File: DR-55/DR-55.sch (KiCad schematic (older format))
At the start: 0 parts

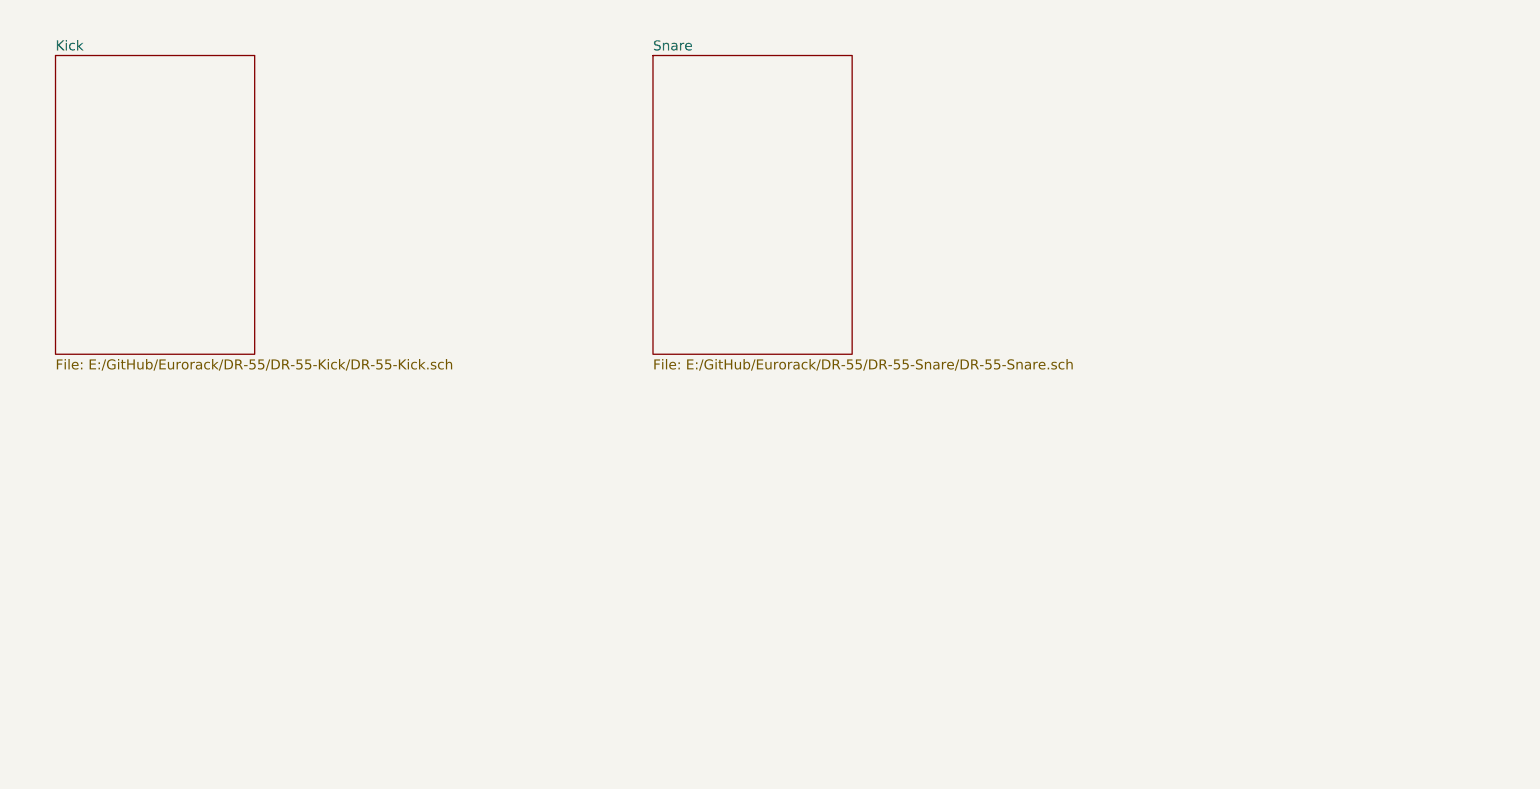
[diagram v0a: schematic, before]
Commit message: Added drums
Added all drum schematics.
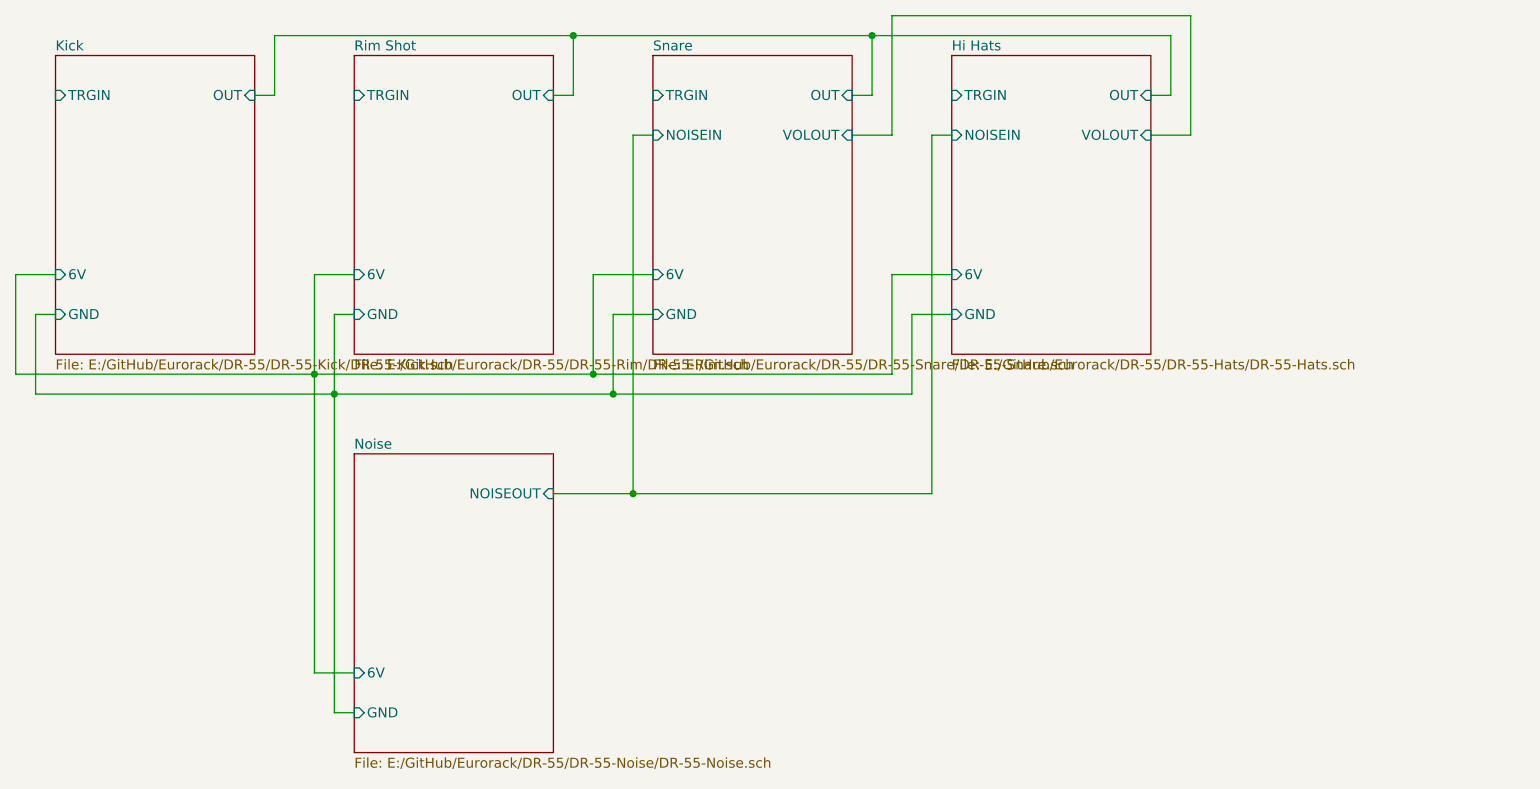
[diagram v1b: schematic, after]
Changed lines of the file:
@@
 $Descr A4 11693 8268
 encoding utf-8
-Sheet 1 3
+Sheet 1 6
 Title ""
 Date ""
@@
 F0 "Kick" 50
 F1 "E:/GitHub/Eurorack/DR-55/DR-55-Kick/DR-55-Kick.sch" 50
+F2 "OUT" I R 2500 1700 50
+F3 "TRGIN" I L 1500 1700 50
+F4 "6V" I L 1500 2600 50
+F5 "GND" I L 1500 2800 50
 $EndSheet
 $Sheet
@@
 F0 "Snare" 50
 F1 "E:/GitHub/Eurorack/DR-55/DR-55-Snare/DR-55-Snare.sch" 50
+F2 "TRGIN" I L 4500 1700 50
+F3 "GND" I L 4500 2800 50
+F4 "OUT" I R 5500 1700 50
+F5 "6V" I L 4500 2600 50
+F6 "VOLOUT" I R 5500 1900 50
+F7 "NOISEIN" I L 4500 1900 50
 $EndSheet
+$Sheet
+S 6000 1500 1000 1500
+U 627D8A3A
+F0 "Hi Hats" 50
+F1 "E:/GitHub/Eurorack/DR-55/DR-55-Hats/DR-55-Hats.sch" 50
+F2 "TRGIN" I L 6000 1700 50
+F3 "GND" I L 6000 2800 50
+F4 "NOISEIN" I L 6000 1900 50
+F5 "OUT" I R 7000 1700 50
+F6 "VOLOUT" I R 7000 1900 50
+F7 "6V" I L 6000 2600 50
+$EndSheet
+$Sheet
+S 3000 3500 1000 1500
+U 62804B1F
+F0 "Noise" 50
+F1 "E:/GitHub/Eurorack/DR-55/DR-55-Noise/DR-55-Noise.sch" 50
+F2 "GND" I L 3000 4800 50
+F3 "6V" I L 3000 4600 50
+F4 "NOISEOUT" I R 4000 3700 50
+$EndSheet
+Wire Wire Line
+	4400 3700 4000 3700
+Wire Wire Line
+	4400 3700 4400 1900
+Wire Wire Line
+	4400 1900 4500 1900
+Wire Wire Line
+	4400 3700 5900 3700
+Wire Wire Line
+	5900 3700 5900 1900
+Wire Wire Line
+	5900 1900 6000 1900
+Connection ~ 4400 3700
+Wire Wire Line
+	1500 2600 1300 2600
+Wire Wire Line
+	1300 2600 1300 3100
+Wire Wire Line
+	5700 3100 5700 2600
+Wire Wire Line
+	5700 2600 6000 2600
+Wire Wire Line
+	1300 3100 2800 3100
+Wire Wire Line
+	3000 2600 2800 2600
+Wire Wire Line
+	2800 2600 2800 3100
+Connection ~ 2800 3100
+Wire Wire Line
+	3000 2800 2900 2800
+Wire Wire Line
+	2900 2800 2900 3200
+Wire Wire Line
+	2900 3200 1400 3200
+Wire Wire Line
+	1400 3200 1400 2800
+Wire Wire Line
+	1400 2800 1500 2800
+$Sheet
+S 3000 1500 1000 1500
+U 62804339
+F0 "Rim Shot" 50
+F1 "E:/GitHub/Eurorack/DR-55/DR-55-Rim/DR-55-Rim.sch" 50
+F2 "TRGIN" I L 3000 1700 50
+F3 "GND" I L 3000 2800 50
+F4 "OUT" I R 4000 1700 50
+F5 "6V" I L 3000 2600 50
+$EndSheet
+Wire Wire Line
+	2800 3100 4200 3100
+Wire Wire Line
+	4500 2600 4200 2600
+Wire Wire Line
+	4200 2600 4200 3100
+Connection ~ 4200 3100
+Wire Wire Line
+	4200 3100 5700 3100
+Wire Wire Line
+	4500 2800 4300 2800
+Wire Wire Line
+	4300 2800 4300 3200
+Wire Wire Line
+	4300 3200 2900 3200
+Connection ~ 2900 3200
+Wire Wire Line
+	4300 3200 5800 3200
+Wire Wire Line
+	5800 3200 5800 2800
+Wire Wire Line
+	5800 2800 6000 2800
+Connection ~ 4300 3200
+Wire Wire Line
+	2500 1700 2600 1700
+Wire Wire Line
+	2600 1700 2600 1400
+Wire Wire Line
+	2600 1400 4100 1400
+Wire Wire Line
+	4100 1400 4100 1700
+Wire Wire Line
+	4100 1700 4000 1700
+Wire Wire Line
+	4100 1400 5600 1400
+Wire Wire Line
+	5600 1400 5600 1700
+Wire Wire Line
+	5600 1700 5500 1700
+Connection ~ 4100 1400
+Wire Wire Line
+	5600 1400 7100 1400
+Wire Wire Line
+	7100 1400 7100 1700
+Wire Wire Line
+	7100 1700 7000 1700
+Connection ~ 5600 1400
+Wire Wire Line
+	7000 1900 7200 1900
+Wire Wire Line
+	7200 1900 7200 1300
+Wire Wire Line
+	7200 1300 5700 1300
+Wire Wire Line
+	5700 1900 5700 1300
+Wire Wire Line
+	5500 1900 5700 1900
+Wire Wire Line
+	3000 4600 2800 4600
+Wire Wire Line
+	2800 4600 2800 3100
+Wire Wire Line
+	3000 4800 2900 4800
+Wire Wire Line
+	2900 4800 2900 3200
 $EndSCHEMATC

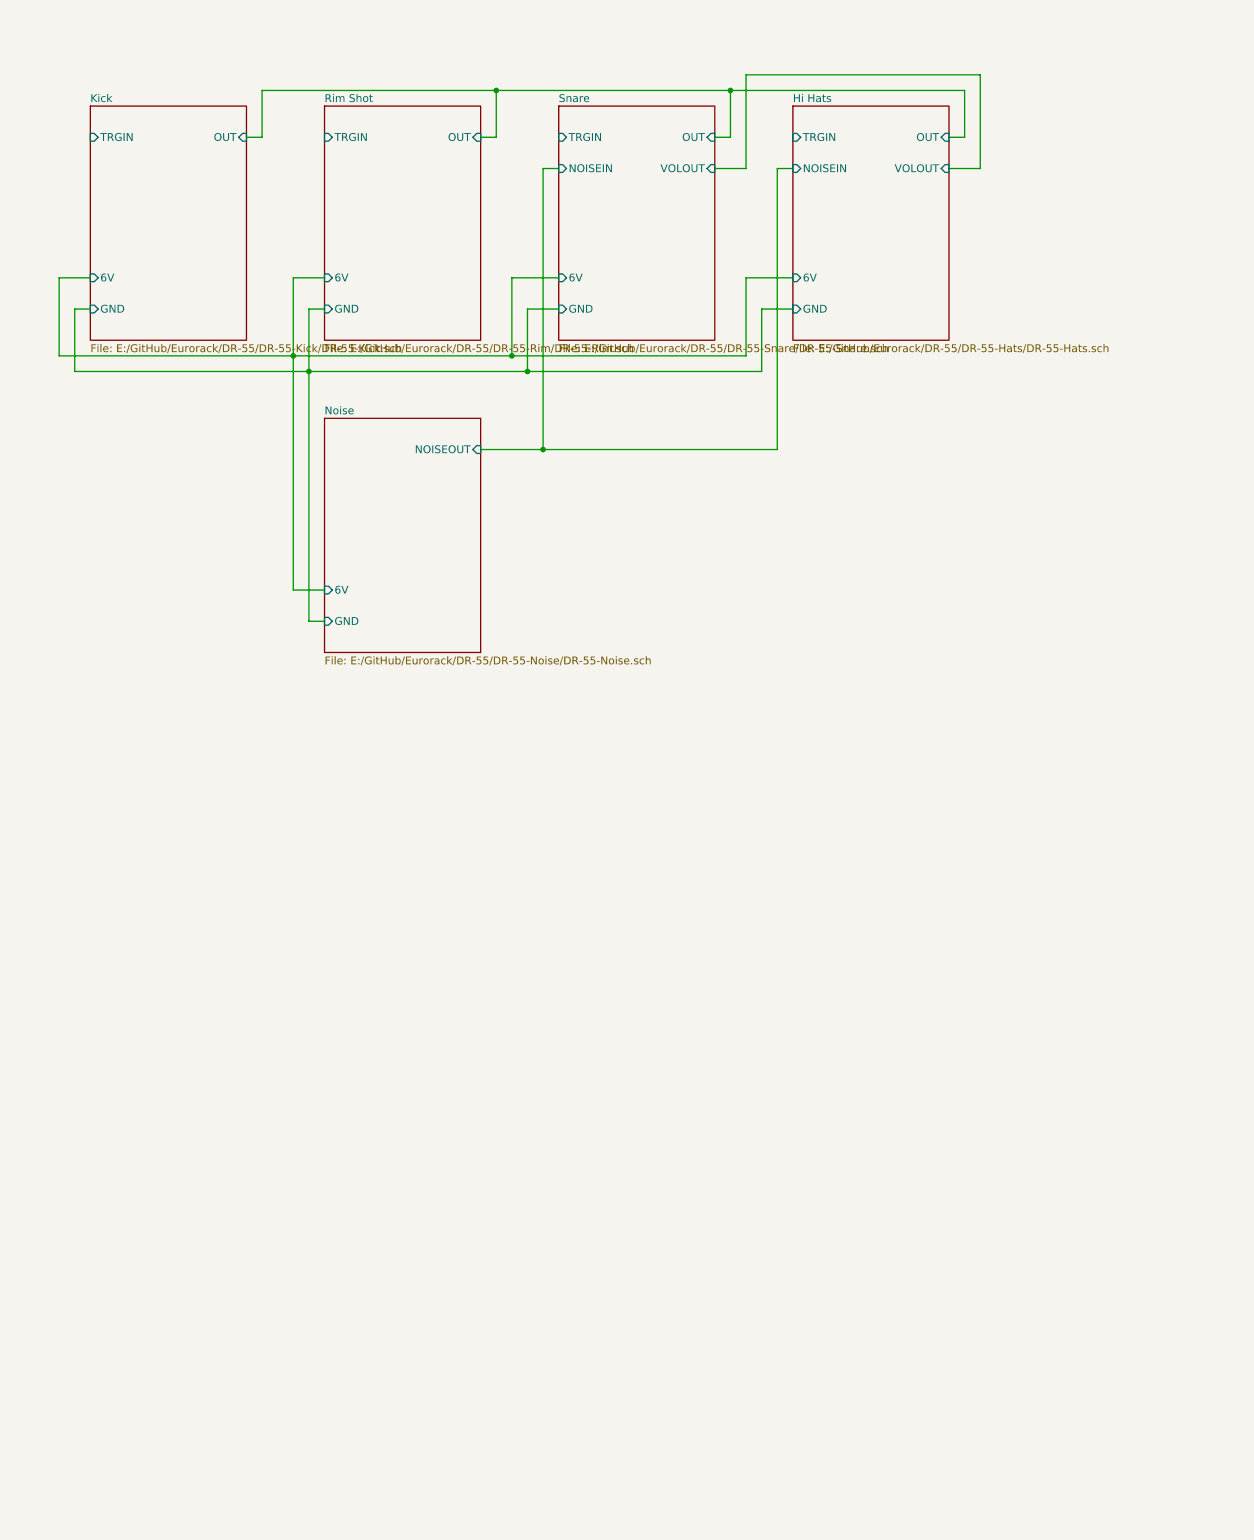
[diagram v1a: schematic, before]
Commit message: rearrange submodules
rearrange hirachial schematics in the main view.
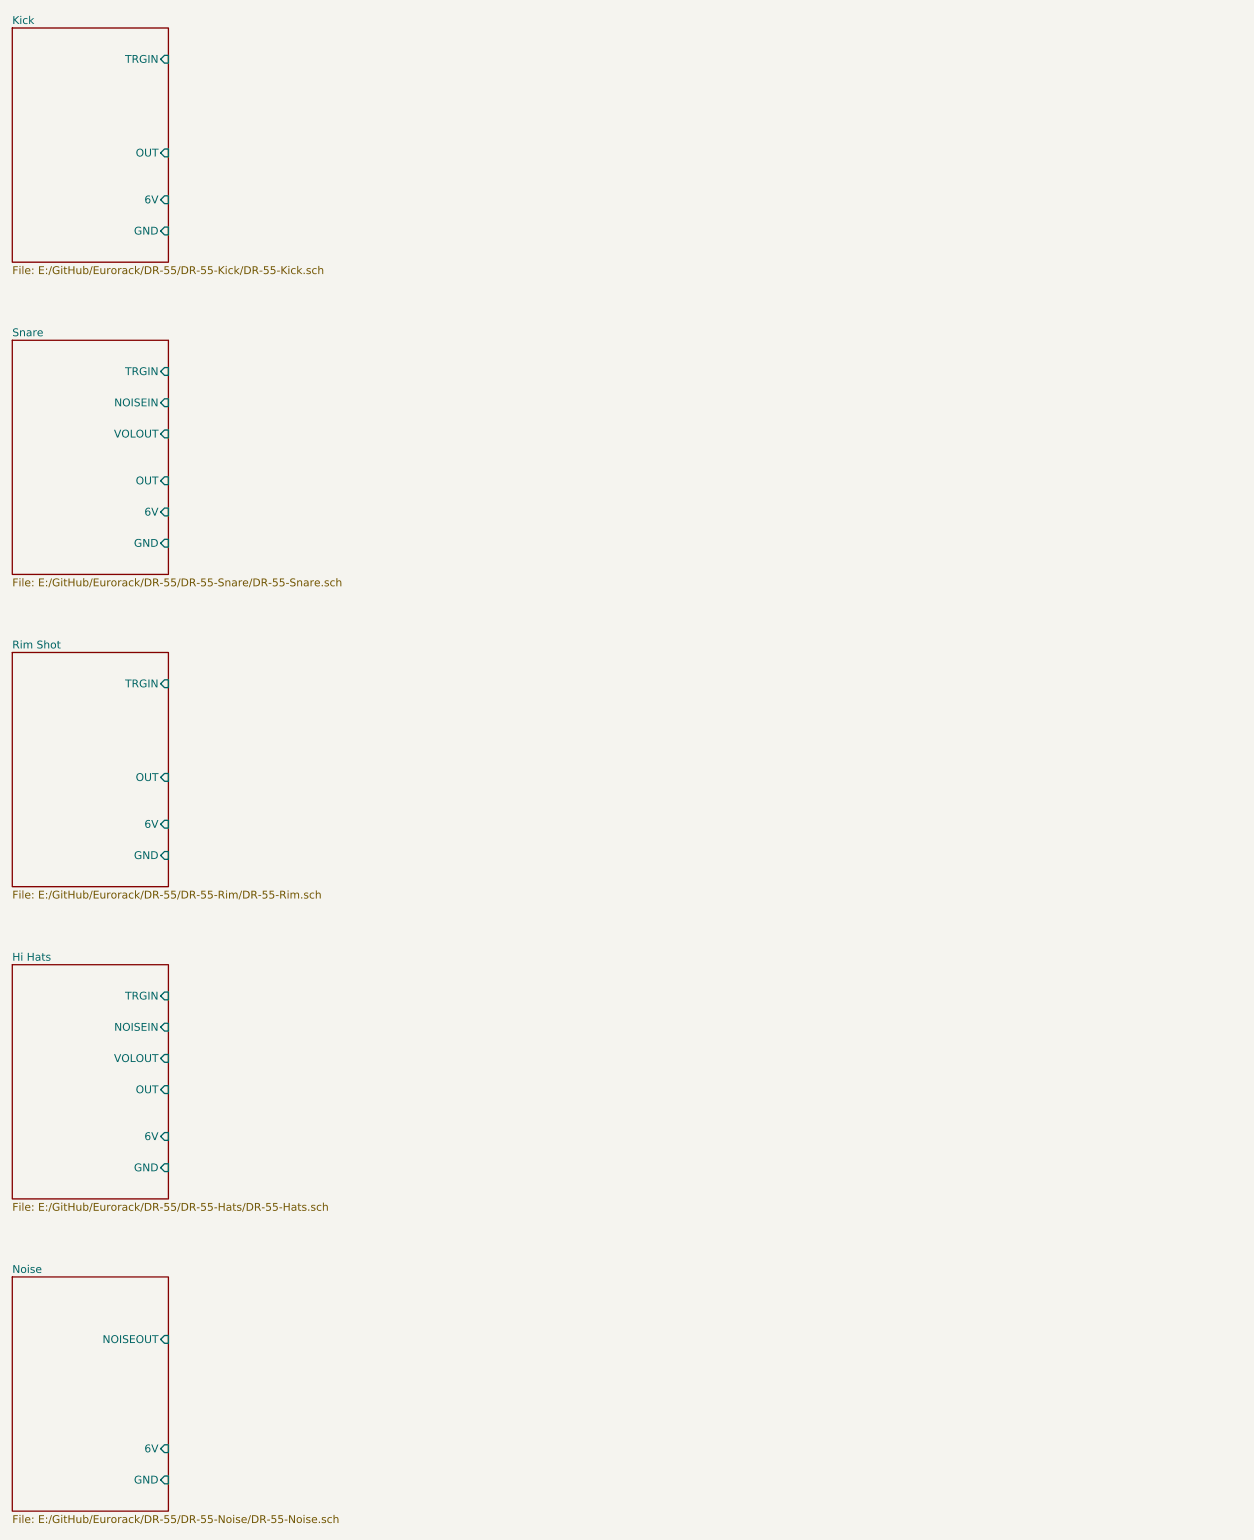
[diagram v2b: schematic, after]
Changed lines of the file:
@@
 EELAYER 30 0
 EELAYER END
-$Descr A4 11693 8268
+$Descr A3 16535 11693
 encoding utf-8
 Sheet 1 6
@@
 $EndDescr
 $Sheet
-S 1500 1500 1000 1500
+S 1000 1000 1000 1500
 U 6276643A
 F0 "Kick" 50
 F1 "E:/GitHub/Eurorack/DR-55/DR-55-Kick/DR-55-Kick.sch" 50
-F2 "OUT" I R 2500 1700 50
-F3 "TRGIN" I L 1500 1700 50
-F4 "6V" I L 1500 2600 50
-F5 "GND" I L 1500 2800 50
+F2 "OUT" I R 2000 1800 50
+F3 "TRGIN" I R 2000 1200 50
+F4 "6V" I R 2000 2100 50
+F5 "GND" I R 2000 2300 50
 $EndSheet
 $Sheet
-S 4500 1500 1000 1500
+S 1000 3000 1000 1500
 U 62740CD0
 F0 "Snare" 50
 F1 "E:/GitHub/Eurorack/DR-55/DR-55-Snare/DR-55-Snare.sch" 50
-F2 "TRGIN" I L 4500 1700 50
-F3 "GND" I L 4500 2800 50
-F4 "OUT" I R 5500 1700 50
-F5 "6V" I L 4500 2600 50
-F6 "VOLOUT" I R 5500 1900 50
-F7 "NOISEIN" I L 4500 1900 50
+F2 "TRGIN" I R 2000 3200 50
+F3 "GND" I R 2000 4300 50
+F4 "OUT" I R 2000 3900 50
+F5 "6V" I R 2000 4100 50
+F6 "VOLOUT" I R 2000 3600 50
+F7 "NOISEIN" I R 2000 3400 50
 $EndSheet
 $Sheet
-S 6000 1500 1000 1500
+S 1000 7000 1000 1500
 U 627D8A3A
 F0 "Hi Hats" 50
 F1 "E:/GitHub/Eurorack/DR-55/DR-55-Hats/DR-55-Hats.sch" 50
-F2 "TRGIN" I L 6000 1700 50
-F3 "GND" I L 6000 2800 50
-F4 "NOISEIN" I L 6000 1900 50
-F5 "OUT" I R 7000 1700 50
-F6 "VOLOUT" I R 7000 1900 50
-F7 "6V" I L 6000 2600 50
+F2 "TRGIN" I R 2000 7200 50
+F3 "GND" I R 2000 8300 50
+F4 "NOISEIN" I R 2000 7400 50
+F5 "OUT" I R 2000 7800 50
+F6 "VOLOUT" I R 2000 7600 50
+F7 "6V" I R 2000 8100 50
 $EndSheet
 $Sheet
-S 3000 3500 1000 1500
+S 1000 5000 1000 1500
+U 62804339
+F0 "Rim Shot" 50
+F1 "E:/GitHub/Eurorack/DR-55/DR-55-Rim/DR-55-Rim.sch" 50
+F2 "TRGIN" I R 2000 5200 50
+F3 "GND" I R 2000 6300 50
+F4 "OUT" I R 2000 5800 50
+F5 "6V" I R 2000 6100 50
+$EndSheet
+$Sheet
+S 1000 9000 1000 1500
 U 62804B1F
 F0 "Noise" 50
 F1 "E:/GitHub/Eurorack/DR-55/DR-55-Noise/DR-55-Noise.sch" 50
-F2 "GND" I L 3000 4800 50
-F3 "6V" I L 3000 4600 50
-F4 "NOISEOUT" I R 4000 3700 50
+F2 "GND" I R 2000 10300 50
+F3 "6V" I R 2000 10100 50
+F4 "NOISEOUT" I R 2000 9400 50
 $EndSheet
-Wire Wire Line
-	4400 3700 4000 3700
-Wire Wire Line
-	4400 3700 4400 1900
-Wire Wire Line
-	4400 1900 4500 1900
-Wire Wire Line
-	4400 3700 5900 3700
-Wire Wire Line
-	5900 3700 5900 1900
-Wire Wire Line
-	5900 1900 6000 1900
-Connection ~ 4400 3700
-Wire Wire Line
-	1500 2600 1300 2600
-Wire Wire Line
-	1300 2600 1300 3100
-Wire Wire Line
-	5700 3100 5700 2600
-Wire Wire Line
-	5700 2600 6000 2600
-Wire Wire Line
-	1300 3100 2800 3100
-Wire Wire Line
-	3000 2600 2800 2600
-Wire Wire Line
-	2800 2600 2800 3100
-Connection ~ 2800 3100
-Wire Wire Line
-	3000 2800 2900 2800
-Wire Wire Line
-	2900 2800 2900 3200
-Wire Wire Line
-	2900 3200 1400 3200
-Wire Wire Line
-	1400 3200 1400 2800
-Wire Wire Line
-	1400 2800 1500 2800
-$Sheet
-S 3000 1500 1000 1500
-U 62804339
-F0 "Rim Shot" 50
-F1 "E:/GitHub/Eurorack/DR-55/DR-55-Rim/DR-55-Rim.sch" 50
-F2 "TRGIN" I L 3000 1700 50
-F3 "GND" I L 3000 2800 50
-F4 "OUT" I R 4000 1700 50
-F5 "6V" I L 3000 2600 50
-$EndSheet
-Wire Wire Line
-	2800 3100 4200 3100
-Wire Wire Line
-	4500 2600 4200 2600
-Wire Wire Line
-	4200 2600 4200 3100
-Connection ~ 4200 3100
-Wire Wire Line
-	4200 3100 5700 3100
-Wire Wire Line
-	4500 2800 4300 2800
-Wire Wire Line
-	4300 2800 4300 3200
-Wire Wire Line
-	4300 3200 2900 3200
-Connection ~ 2900 3200
-Wire Wire Line
-	4300 3200 5800 3200
-Wire Wire Line
-	5800 3200 5800 2800
-Wire Wire Line
-	5800 2800 6000 2800
-Connection ~ 4300 3200
-Wire Wire Line
-	2500 1700 2600 1700
-Wire Wire Line
-	2600 1700 2600 1400
-Wire Wire Line
-	2600 1400 4100 1400
-Wire Wire Line
-	4100 1400 4100 1700
-Wire Wire Line
-	4100 1700 4000 1700
-Wire Wire Line
-	4100 1400 5600 1400
-Wire Wire Line
-	5600 1400 5600 1700
-Wire Wire Line
-	5600 1700 5500 1700
-Connection ~ 4100 1400
-Wire Wire Line
-	5600 1400 7100 1400
-Wire Wire Line
-	7100 1400 7100 1700
-Wire Wire Line
-	7100 1700 7000 1700
-Connection ~ 5600 1400
-Wire Wire Line
-	7000 1900 7200 1900
-Wire Wire Line
-	7200 1900 7200 1300
-Wire Wire Line
-	7200 1300 5700 1300
-Wire Wire Line
-	5700 1900 5700 1300
-Wire Wire Line
-	5500 1900 5700 1900
-Wire Wire Line
-	3000 4600 2800 4600
-Wire Wire Line
-	2800 4600 2800 3100
-Wire Wire Line
-	3000 4800 2900 4800
-Wire Wire Line
-	2900 4800 2900 3200
 $EndSCHEMATC
